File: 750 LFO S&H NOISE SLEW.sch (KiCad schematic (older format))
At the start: 234 parts, among them J1 JACK_MONO_SW, J10 JACK_MONO_SW, J11 JACK_MONO_SW, J2 JACK_MONO_SW, J3 JACK_MONO_SW, J4 JACK_MONO_SW, J5 JACK_MONO_SW, J6 JACK_MONO_SW, J7 JACK_MONO_SW, J8 JACK_MONO_SW, J9 JACK_MONO_SW, P1 CONN_02X01, P2 CONN_02X01, P3 CONN_02X05, Q1 MMBT3904, Q10 MMBT3904, Q11 J112, Q12 MMBT3906, Q13 J112, Q14 J112, Q15 MMBT3904, Q16 MMBT3904, Q2 MMBT3904, Q3 2N7002, Q4 2N7002, Q5 MBT3946DW, Q6 DMMT3904W, Q7 MMBT3904, Q8 MMBT3904, Q9 MMBT3904, SW1 KS-01Q, SW2 KS-01Q, U1 LM13700, U10 TL072-, U11 TL072-, U12 MAX9945, U13 DG409, U14 DG409, U2 TL072-, U3 TL072-, U4 TL072-, U5 TL072-, U6 CD40106, U7 CD4027, U8 CD4027, U9 TL072-

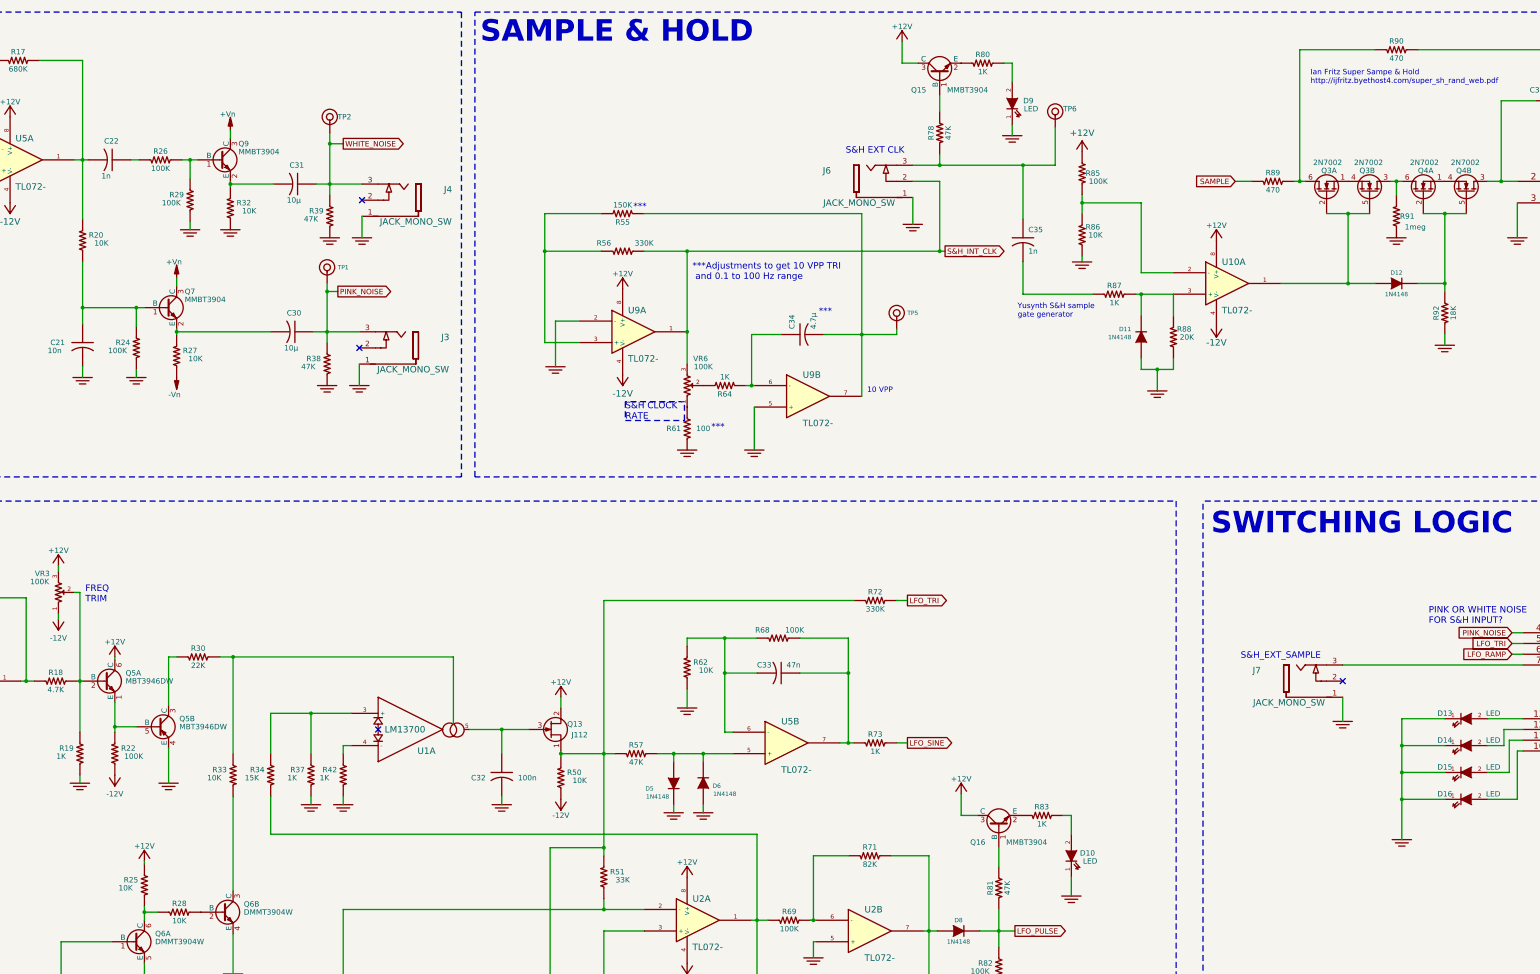
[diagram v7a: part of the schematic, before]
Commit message: added notes to schematic based on building first prototype
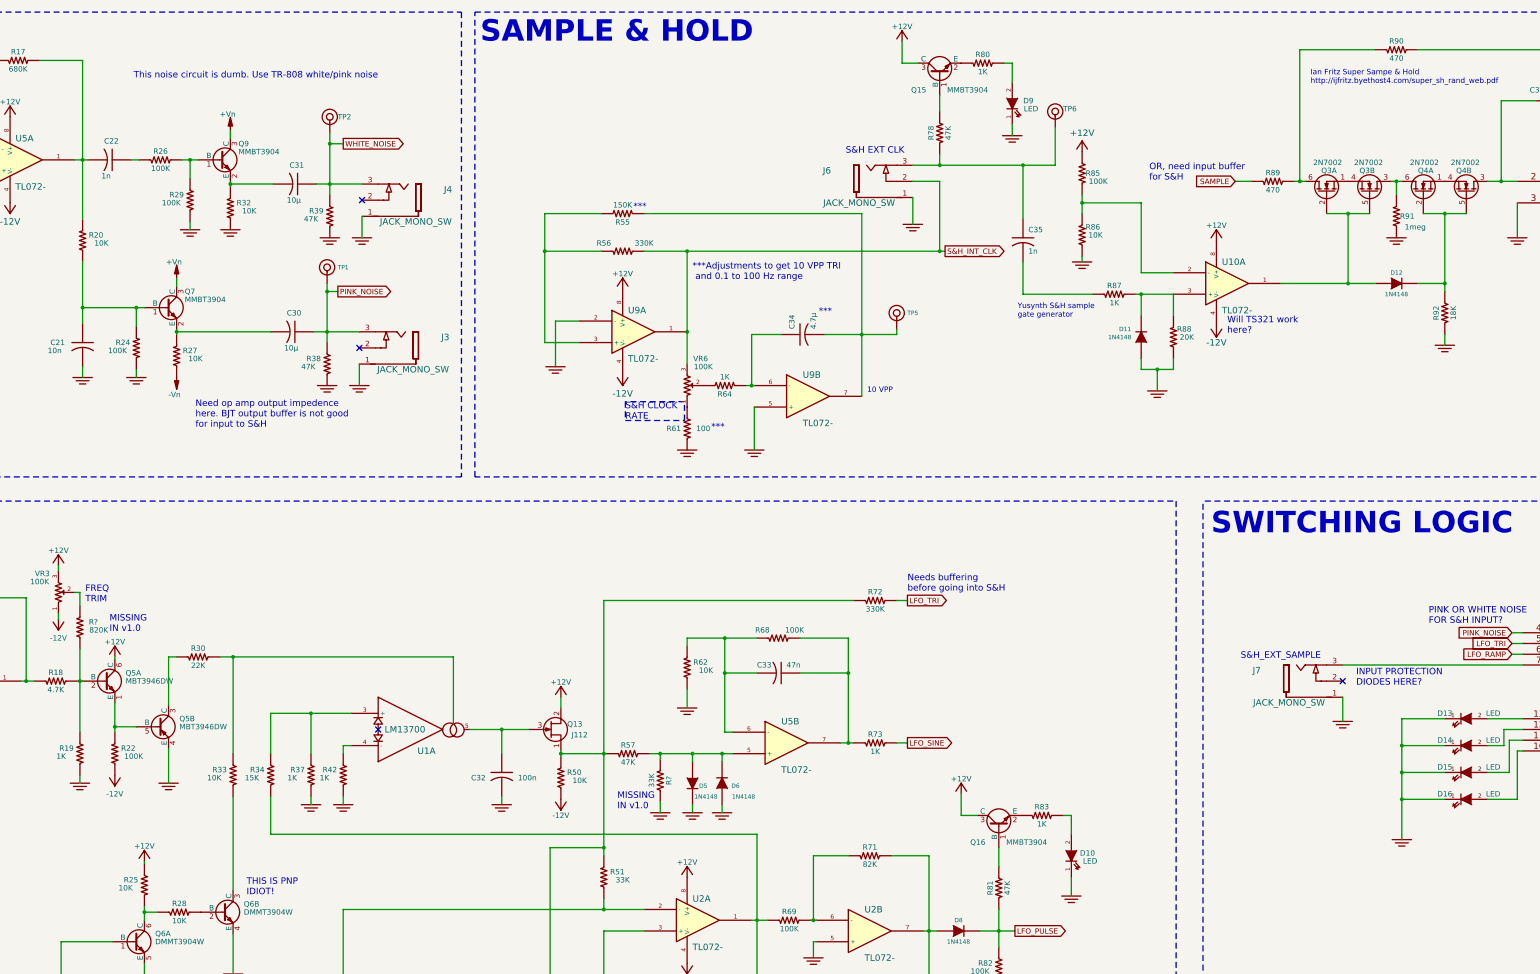
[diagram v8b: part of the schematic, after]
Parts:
- added R?: 33K, MyModules:SM0603-R-JRL, symbol R_US
- added R?: 820K, MyModules:SM0603-R-JRL, symbol R_US
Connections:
- net GND: now also R?.2
- net at Q5.2 (B), R18.2, R19.1: now also R?.2; no longer VR3.2
- net at D5.1 (A), D6.2 (K), R57.2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: now also R?.1
- new net: R?.1, VR3.2
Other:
- note added: "INPUT PROTECTION\nDIODES HERE?"
- note added: "MISSING\nIN v1.0"
- note added: "Need op amp output impedence\nhere. BJT output buffer is not good\nfor input to S&H"
- note added: "Needs buffering\nbefore going into S&H\n"
- note added: "OR, need input buffer \nfor S&H"
- note added: "THIS IS PNP\nIDIOT!"
- note added: "This noise circuit is dumb. Use TR-808 white/pink noise"
- note added: "Will TS321 work\nhere?"
- moved on the sheet: D5, D6, R57
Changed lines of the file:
@@
 	4500 8575 4500 8650
 Wire Wire Line
-	4500 6875 4500 8175
-Wire Wire Line
 	4475 7700 4525 7700
 Connection ~ 4500 7700
@@
 L DIODE D5
 U 1 1 56F8818C
-P 10025 8650
-F 0 "D5" V 10075 8425 40  0000 C CNN
-F 1 "1N4148" V 10150 8500 40  0000 C CNN
-F 2 "MyModules:SOD323-JRL" H 10025 8650 60  0001 C CNN
-F 3 "~" H 10025 8650 60  0000 C CNN
-	1    10025 8650
+P 10200 8650
+F 0 "D5" V 10225 8750 40  0000 C CNN
+F 1 "1N4148" V 10325 8775 40  0000 C CNN
+F 2 "MyModules:SOD323-JRL" H 10200 8650 60  0001 C CNN
+F 3 "~" H 10200 8650 60  0000 C CNN
+	1    10200 8650
 	0    1    1    0
 $EndComp
@@
 L R_US R57
 U 1 1 56F8A38D
-P 9675 8375
-F 0 "R57" V 9755 8375 50  0000 C CNN
-F 1 "47K" V 9595 8375 50  0000 C CNN
-F 2 "MyModules:SM0603-R-JRL" H 9675 8375 60  0001 C CNN
-F 3 "" H 9675 8375 60  0000 C CNN
-	1    9675 8375
+P 9600 8375
+F 0 "R57" V 9680 8375 50  0000 C CNN
+F 1 "47K" V 9520 8375 50  0000 C CNN
+F 2 "MyModules:SM0603-R-JRL" H 9600 8375 60  0001 C CNN
+F 3 "" H 9600 8375 60  0000 C CNN
+	1    9600 8375
 	0    -1   -1   0
 $EndComp
 Wire Wire Line
-	8975 8375 9475 8375
+	8975 8375 9400 8375
 Connection ~ 8975 8375
 $Comp
@@
 L GND_E #PWR096
 U 1 1 56F8DA53
-P 10025 8925
-F 0 "#PWR096" V 10025 8925 30  0001 C CNN
-F 1 "GND_E" H 10025 8855 30  0001 C CNN
-F 2 "" H 10025 8925 60  0000 C CNN
-F 3 "" H 10025 8925 60  0000 C CNN
-	1    10025 8925
+P 10200 8925
+F 0 "#PWR096" V 10200 8925 30  0001 C CNN
+F 1 "GND_E" H 10200 8855 30  0001 C CNN
+F 2 "" H 10200 8925 60  0000 C CNN
+F 3 "" H 10200 8925 60  0000 C CNN
+	1    10200 8925
 	1    0    0    -1
 $EndComp
 Wire Wire Line
-	9875 8375 10575 8375
+	9800 8375 10575 8375
 Wire Wire Line
-	10025 8375 10025 8450
+	10200 8375 10200 8450
 Wire Wire Line
-	10025 8850 10025 8925
+	10200 8850 10200 8925
 $Comp
 L DIODE D6
 U 1 1 56F8E477
-P 10300 8650
-F 0 "D6" V 10275 8525 40  0000 C CNN
-F 1 "1N4148" V 10200 8450 40  0000 C CNN
-F 2 "MyModules:SOD323-JRL" H 10300 8650 60  0001 C CNN
-F 3 "~" H 10300 8650 60  0000 C CNN
-	1    10300 8650
+P 10475 8650
+F 0 "D6" V 10450 8525 40  0000 C CNN
+F 1 "1N4148" V 10350 8450 40  0000 C CNN
+F 2 "MyModules:SOD323-JRL" H 10475 8650 60  0001 C CNN
+F 3 "~" H 10475 8650 60  0000 C CNN
+	1    10475 8650
 	0    -1   -1   0
 $EndComp
@@
 L GND_E #PWR097
 U 1 1 56F8E47D
-P 10300 8925
-F 0 "#PWR097" V 10300 8925 30  0001 C CNN
-F 1 "GND_E" H 10300 8855 30  0001 C CNN
-F 2 "" H 10300 8925 60  0000 C CNN
-F 3 "" H 10300 8925 60  0000 C CNN
-	1    10300 8925
+P 10475 8925
+F 0 "#PWR097" V 10475 8925 30  0001 C CNN
+F 1 "GND_E" H 10475 8855 30  0001 C CNN
+F 2 "" H 10475 8925 60  0000 C CNN
+F 3 "" H 10475 8925 60  0000 C CNN
+	1    10475 8925
 	1    0    0    -1
 $EndComp
 Wire Wire Line
-	10300 8375 10300 8450
+	10475 8375 10475 8450
 Wire Wire Line
-	10300 8850 10300 8925
-Connection ~ 10025 8375
-Connection ~ 10300 8375
+	10475 8850 10475 8925
+Connection ~ 10200 8375
+Connection ~ 10475 8375
 $Comp
 L R_US R68
@@
 Text Notes 10150 13600 2    60   ~ 0
 *double check\nQ14 footprint
+$Comp
+L R_US R?
+U 1 1 584CCA9E
+P 9900 8625
+F 0 "R?" V 9980 8625 50  0000 C CNN
+F 1 "33K" V 9820 8625 50  0000 C CNN
+F 2 "MyModules:SM0603-R-JRL" H 9900 8625 60  0001 C CNN
+F 3 "" H 9900 8625 60  0000 C CNN
+	1    9900 8625
+	1    0    0    -1
+$EndComp
+$Comp
+L GND_E #PWR?
+U 1 1 584CCDCC
+P 9900 8925
+F 0 "#PWR?" V 9900 8925 30  0001 C CNN
+F 1 "GND_E" H 9900 8855 30  0001 C CNN
+F 2 "" H 9900 8925 60  0000 C CNN
+F 3 "" H 9900 8925 60  0000 C CNN
+	1    9900 8925
+	1    0    0    -1
+$EndComp
+Wire Wire Line
+	9900 8925 9900 8825
+Wire Wire Line
+	9900 8425 9900 8375
+Connection ~ 9900 8375
+Text Notes 9500 8900 0    60   ~ 0
+MISSING\nIN v1.0
+$Comp
+L R_US R?
+U 1 1 584EAFFF
+P 4500 7200
+F 0 "R?" H 4625 7250 50  0000 C CNN
+F 1 "820K" H 4675 7175 50  0000 C CNN
+F 2 "MyModules:SM0603-R-JRL" H 4500 7200 60  0001 C CNN
+F 3 "" H 4500 7200 60  0000 C CNN
+	1    4500 7200
+	1    0    0    -1
+$EndComp
+Wire Wire Line
+	4500 6875 4500 7000
+Wire Wire Line
+	4500 7400 4500 8175
+Text Notes 4775 7250 0    60   ~ 0
+MISSING\nIN v1.0
+Text Notes 12200 6875 0    60   ~ 0
+Needs buffering\nbefore going into S&H\n
+Text Notes 5000 2100 0    60   ~ 0
+This noise circuit is dumb. Use TR-808 white/pink noise
+Text Notes 5575 5350 0    60   ~ 0
+Need op amp output impedence\nhere. BJT output buffer is not good\nfor input to S&H
+Text Notes 14450 3050 0    60   ~ 0
+OR, need input buffer \nfor S&H
+Text Notes 15175 4475 0    60   ~ 0
+Will TS321 work\nhere?
+Text Notes 6050 9700 0    60   ~ 0
+THIS IS PNP\nIDIOT!
+Text Notes 16375 7750 0    60   ~ 0
+INPUT PROTECTION\nDIODES HERE?
 $EndSCHEMATC
